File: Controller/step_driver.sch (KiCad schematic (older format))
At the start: 4 parts

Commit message: Minor update to stepper
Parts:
- removed J?: Conn_01x04_Female, symbol Connector:Conn_01x04_Female
- added CN? (x3): CFG1, OPL_Connector:H3-2.54, symbol OPL_Connector:DIP-BLACK-MALE-HEADER-VERT_3P-2.54_
- added J?: Conn_01x04_Male, symbol Connector:Conn_01x04_Male
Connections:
- net labels added: CFG1, CFG2, CFG3
- wire segments 11 -> 14
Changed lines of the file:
@@
 Wire Wire Line
 	3800 2950 3800 3050
-$Comp
-L Connector:Conn_01x04_Female J?
-U 1 1 5D4B72EB
-P 6150 2850
-F 0 "J?" H 6178 2826 50  0000 L CNN
-F 1 "Conn_01x04_Female" H 6178 2735 50  0000 L CNN
-F 2 "" H 6150 2850 50  0001 C CNN
-F 3 "~" H 6150 2850 50  0001 C CNN
-	1    6150 2850
-	1    0    0    -1
-$EndComp
 Wire Wire Line
 	5650 2750 5950 2750
@@
 Wire Wire Line
 	5850 3150 5650 3150
+$Comp
+L Connector:Conn_01x04_Male J?
+U 1 1 5D4B9EAC
+P 6150 2850
+F 0 "J?" H 6122 2824 50  0000 R CNN
+F 1 "Conn_01x04_Male" H 6122 2733 50  0000 R CNN
+F 2 "" H 6150 2850 50  0001 C CNN
+F 3 "~" H 6150 2850 50  0001 C CNN
+	1    6150 2850
+	-1   0    0    -1
+$EndComp
+Text Label 3600 2650 0    31   ~ 0
+CFG1
+Text Label 3600 2750 0    31   ~ 0
+CFG2
+Text Label 3600 2850 0    31   ~ 0
+CFG3
+Wire Wire Line
+	3600 2650 3800 2650
+Wire Wire Line
+	3800 2750 3600 2750
+Wire Wire Line
+	3600 2850 3800 2850
+Text Label 2650 2150 3    31   ~ 0
+CFG1
+Text GLabel 2500 2150 3    31   Input ~ 0
+5V
+$Comp
+L power:GND #PWR?
+U 1 1 5D4BCF63
+P 2800 2150
+F 0 "#PWR?" H 2800 1900 50  0001 C CNN
+F 1 "GND" H 2805 1977 50  0000 C CNN
+F 2 "" H 2800 2150 50  0001 C CNN
+F 3 "" H 2800 2150 50  0001 C CNN
+	1    2800 2150
+	1    0    0    -1
+$EndComp
+$Comp
+L OPL_Connector:DIP-BLACK-MALE-HEADER-VERT_3P-2.54_ CN?
+U 1 1 5D4BDC37
+P 2650 2500
+F 0 "CN?" V 2584 2272 45  0000 R CNN
+F 1 "CFG1" V 2500 2272 45  0000 R CNN
+F 2 "OPL_Connector:H3-2.54" H 2650 2500 50  0001 C CNN
+F 3 "" H 2650 2500 50  0001 C CNN
+F 4 "320020079" H 2680 2650 20  0001 C CNN "SKU"
+	1    2650 2500
+	0    -1   -1   0
+$EndComp
+Text Label 2650 2800 3    31   ~ 0
+CFG2
+Text GLabel 2500 2800 3    31   Input ~ 0
+5V
+$Comp
+L power:GND #PWR?
+U 1 1 5D4BDC43
+P 2800 2800
+F 0 "#PWR?" H 2800 2550 50  0001 C CNN
+F 1 "GND" H 2805 2627 50  0000 C CNN
+F 2 "" H 2800 2800 50  0001 C CNN
+F 3 "" H 2800 2800 50  0001 C CNN
+	1    2800 2800
+	1    0    0    -1
+$EndComp
+$Comp
+L OPL_Connector:DIP-BLACK-MALE-HEADER-VERT_3P-2.54_ CN?
+U 1 1 5D4BEA96
+P 2650 3150
+F 0 "CN?" V 2584 2922 45  0000 R CNN
+F 1 "CFG1" V 2500 2922 45  0000 R CNN
+F 2 "OPL_Connector:H3-2.54" H 2650 3150 50  0001 C CNN
+F 3 "" H 2650 3150 50  0001 C CNN
+F 4 "320020079" H 2680 3300 20  0001 C CNN "SKU"
+	1    2650 3150
+	0    -1   -1   0
+$EndComp
+Text Label 2650 3450 3    31   ~ 0
+CFG3
+Text GLabel 2500 3450 3    31   Input ~ 0
+5V
+$Comp
+L power:GND #PWR?
+U 1 1 5D4BEAA2
+P 2800 3450
+F 0 "#PWR?" H 2800 3200 50  0001 C CNN
+F 1 "GND" H 2805 3277 50  0000 C CNN
+F 2 "" H 2800 3450 50  0001 C CNN
+F 3 "" H 2800 3450 50  0001 C CNN
+	1    2800 3450
+	1    0    0    -1
+$EndComp
+$Comp
+L OPL_Connector:DIP-BLACK-MALE-HEADER-VERT_3P-2.54_ CN?
+U 1 1 5D4BBA78
+P 2650 1850
+F 0 "CN?" V 2584 1622 45  0000 R CNN
+F 1 "CFG1" V 2500 1622 45  0000 R CNN
+F 2 "OPL_Connector:H3-2.54" H 2650 1850 50  0001 C CNN
+F 3 "" H 2650 1850 50  0001 C CNN
+F 4 "320020079" H 2680 2000 20  0001 C CNN "SKU"
+	1    2650 1850
+	0    -1   -1   0
+$EndComp
 $EndSCHEMATC

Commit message: Almost complete schematic
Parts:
- removed J?: Conn_01x04_Male, symbol Connector:Conn_01x04_Male
- added J?: MotorConn, TerminalBlock_Phoenix:TerminalBlock_Phoenix_MPT-0,5-4-2.54_1x04_P2.54mm_Horizontal, symbol Connector:Screw_Terminal_01x04
- C?: value CP1 -> 47uF
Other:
- note added: "!Reset"
- note added: "!Sleep"
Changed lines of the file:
@@
 $Descr A4 11693 8268
 encoding utf-8
-Sheet 3 3
+Sheet 4 4
 Title ""
 Date ""
@@
 U 1 1 5D4B02F5
 P 4100 2900
+AR Path="/5D4AFE00/5D4B02F5" Ref="CN?"  Part="1"
+AR Path="/5D4C0FEF/5D4B02F5" Ref="CN?"  Part="1"
+AR Path="/5D4C1080/5D4B02F5" Ref="CN?"  Part="1"
 F 0 "CN?" H 4228 2942 45  0000 L CNN
 F 1 "FEMALE_LEFT" H 4228 2858 45  0000 L CNN
@@
 U 1 1 5D4B13AD
 P 5350 2900
+AR Path="/5D4AFE00/5D4B13AD" Ref="CN?"  Part="1"
+AR Path="/5D4C0FEF/5D4B13AD" Ref="CN?"  Part="1"
+AR Path="/5D4C1080/5D4B13AD" Ref="CN?"  Part="1"
 F 0 "CN?" H 5700 2950 45  0000 C CNN
 F 1 "FEMALE_RIGHT" H 5700 2850 45  0000 C CNN
@@
 U 1 1 5D4B27F8
 P 5650 2300
+AR Path="/5D4AFE00/5D4B27F8" Ref="C?"  Part="1"
+AR Path="/5D4C0FEF/5D4B27F8" Ref="C?"  Part="1"
+AR Path="/5D4C1080/5D4B27F8" Ref="C?"  Part="1"
 F 0 "C?" H 5535 2254 50  0000 R CNN
-F 1 "CP1" H 5535 2345 50  0000 R CNN
+F 1 "47uF" H 5535 2345 50  0000 R CNN
 F 2 "Capacitor_SMD:CP_Elec_6.3x5.4" H 5650 2300 50  0001 C CNN
 F 3 "~" H 5650 2300 50  0001 C CNN
@@
 U 1 1 5D4B699E
 P 5650 2150
+AR Path="/5D4AFE00/5D4B699E" Ref="#PWR?"  Part="1"
+AR Path="/5D4C0FEF/5D4B699E" Ref="#PWR?"  Part="1"
+AR Path="/5D4C1080/5D4B699E" Ref="#PWR?"  Part="1"
 F 0 "#PWR?" H 5650 1900 50  0001 C CNN
 F 1 "GND" H 5655 1977 50  0000 C CNN
@@
 U 1 1 5D4B88E4
 P 5750 3350
+AR Path="/5D4AFE00/5D4B88E4" Ref="#PWR?"  Part="1"
+AR Path="/5D4C0FEF/5D4B88E4" Ref="#PWR?"  Part="1"
+AR Path="/5D4C1080/5D4B88E4" Ref="#PWR?"  Part="1"
 F 0 "#PWR?" H 5750 3100 50  0001 C CNN
 F 1 "GND" H 5755 3177 50  0000 C CNN
@@
 Wire Wire Line
 	5850 3150 5650 3150
-$Comp
-L Connector:Conn_01x04_Male J?
-U 1 1 5D4B9EAC
-P 6150 2850
-F 0 "J?" H 6122 2824 50  0000 R CNN
-F 1 "Conn_01x04_Male" H 6122 2733 50  0000 R CNN
-F 2 "" H 6150 2850 50  0001 C CNN
-F 3 "~" H 6150 2850 50  0001 C CNN
-	1    6150 2850
-	-1   0    0    -1
-$EndComp
 Text Label 3600 2650 0    31   ~ 0
 CFG1
@@
 U 1 1 5D4BCF63
 P 2800 2150
+AR Path="/5D4AFE00/5D4BCF63" Ref="#PWR?"  Part="1"
+AR Path="/5D4C0FEF/5D4BCF63" Ref="#PWR?"  Part="1"
+AR Path="/5D4C1080/5D4BCF63" Ref="#PWR?"  Part="1"
 F 0 "#PWR?" H 2800 1900 50  0001 C CNN
 F 1 "GND" H 2805 1977 50  0000 C CNN
@@
 U 1 1 5D4BDC37
 P 2650 2500
+AR Path="/5D4AFE00/5D4BDC37" Ref="CN?"  Part="1"
+AR Path="/5D4C0FEF/5D4BDC37" Ref="CN?"  Part="1"
+AR Path="/5D4C1080/5D4BDC37" Ref="CN?"  Part="1"
 F 0 "CN?" V 2584 2272 45  0000 R CNN
 F 1 "CFG1" V 2500 2272 45  0000 R CNN
@@
 U 1 1 5D4BDC43
 P 2800 2800
+AR Path="/5D4AFE00/5D4BDC43" Ref="#PWR?"  Part="1"
+AR Path="/5D4C0FEF/5D4BDC43" Ref="#PWR?"  Part="1"
+AR Path="/5D4C1080/5D4BDC43" Ref="#PWR?"  Part="1"
 F 0 "#PWR?" H 2800 2550 50  0001 C CNN
 F 1 "GND" H 2805 2627 50  0000 C CNN
@@
 U 1 1 5D4BEA96
 P 2650 3150
+AR Path="/5D4AFE00/5D4BEA96" Ref="CN?"  Part="1"
+AR Path="/5D4C0FEF/5D4BEA96" Ref="CN?"  Part="1"
+AR Path="/5D4C1080/5D4BEA96" Ref="CN?"  Part="1"
 F 0 "CN?" V 2584 2922 45  0000 R CNN
 F 1 "CFG1" V 2500 2922 45  0000 R CNN
@@
 U 1 1 5D4BEAA2
 P 2800 3450
+AR Path="/5D4AFE00/5D4BEAA2" Ref="#PWR?"  Part="1"
+AR Path="/5D4C0FEF/5D4BEAA2" Ref="#PWR?"  Part="1"
+AR Path="/5D4C1080/5D4BEAA2" Ref="#PWR?"  Part="1"
 F 0 "#PWR?" H 2800 3200 50  0001 C CNN
 F 1 "GND" H 2805 3277 50  0000 C CNN
@@
 U 1 1 5D4BBA78
 P 2650 1850
+AR Path="/5D4AFE00/5D4BBA78" Ref="CN?"  Part="1"
+AR Path="/5D4C0FEF/5D4BBA78" Ref="CN?"  Part="1"
+AR Path="/5D4C1080/5D4BBA78" Ref="CN?"  Part="1"
 F 0 "CN?" V 2584 1622 45  0000 R CNN
 F 1 "CFG1" V 2500 1622 45  0000 R CNN
@@
 	0    -1   -1   0
 $EndComp
+Text Notes 3650 2950 0    31   ~ 0
+!Reset
+Text Notes 3650 3050 0    31   ~ 0
+!Sleep
+$Comp
+L Connector:Screw_Terminal_01x04 J?
+U 1 1 5D4D9DAD
+P 6150 2850
+AR Path="/5D4D9DAD" Ref="J?"  Part="1"
+AR Path="/5D4AFE00/5D4D9DAD" Ref="J?"  Part="1"
+AR Path="/5D4C1080/5D4D9DAD" Ref="J?"  Part="1"
+F 0 "J?" H 6230 2842 50  0000 L CNN
+F 1 "MotorConn" H 6230 2751 50  0000 L CNN
+F 2 "TerminalBlock_Phoenix:TerminalBlock_Phoenix_MPT-0,5-4-2.54_1x04_P2.54mm_Horizontal" H 6150 2850 50  0001 C CNN
+F 3 "~" H 6150 2850 50  0001 C CNN
+F 4 "320110143" H 6150 2850 50  0001 C CNN "SKU"
+F 5 "GS019-2.54-04P-5" H 6150 2850 50  0001 C CNN "MPN"
+	1    6150 2850
+	1    0    0    -1
+$EndComp
 $EndSCHEMATC

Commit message: Complete schematic
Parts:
- added J?: MotorHeader, symbol OPL_Connector:DIP-BLACK-MALE-HEADER-VERT_4P-2.54_
- CN? (x2): footprint (none) -> OPL_Connector:H8-2.54
- J?: value MotorConn -> MotorTerm
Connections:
- net at CN?.3, J?.1 (Pin_1): now also J?.1 (P$1)
- net at CN?.4, J?.2 (Pin_2): now also J?.2 (P$2)
- net at CN?.5, J?.3 (Pin_3): now also J?.3 (P$3)
- net at CN?.6, J?.4 (Pin_4): now also J?.4 (P$4)
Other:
- note added: "!Enable"
- note added: "CFG1"
- note added: "CFG2"
- note added: "CFG3"
- note added: "Dir"
- note added: "Gnd"
- note added: "MotA+"
- note added: "MotA-"
- note added: "MotB+"
- note added: "MotB-"
- note added: "Step"
- note added: "VMot"
- note added: "Vdd"
- moved on the sheet: J?
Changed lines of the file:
@@
 $Descr A4 11693 8268
 encoding utf-8
-Sheet 4 4
+Sheet 3 4
 Title ""
 Date ""
@@
 AR Path="/5D4C0FEF/5D4B02F5" Ref="CN?"  Part="1"
 AR Path="/5D4C1080/5D4B02F5" Ref="CN?"  Part="1"
-F 0 "CN?" H 4228 2942 45  0000 L CNN
-F 1 "FEMALE_LEFT" H 4228 2858 45  0000 L CNN
-F 2 "" H 4100 2900 50  0001 C CNN
+F 0 "CN?" H 4000 3350 45  0000 L CNN
+F 1 "FEMALE_LEFT" H 4000 2450 45  0000 L CNN
+F 2 "OPL_Connector:H8-2.54" H 4100 2900 50  0001 C CNN
 F 3 "" H 4100 2900 50  0001 C CNN
 F 4 "F185-1108A1BSYC1" H 4130 3050 20  0001 C CNN "MPN"
@@
 AR Path="/5D4C0FEF/5D4B13AD" Ref="CN?"  Part="1"
 AR Path="/5D4C1080/5D4B13AD" Ref="CN?"  Part="1"
-F 0 "CN?" H 5700 2950 45  0000 C CNN
-F 1 "FEMALE_RIGHT" H 5700 2850 45  0000 C CNN
-F 2 "" H 5350 2900 50  0001 C CNN
+F 0 "CN?" H 5300 3350 45  0000 C CNN
+F 1 "FEMALE_RIGHT" H 5500 2450 45  0000 C CNN
+F 2 "OPL_Connector:H8-2.54" H 5350 2900 50  0001 C CNN
 F 3 "" H 5350 2900 50  0001 C CNN
 F 4 "F185-1108A1BSYC1" H 5380 3050 20  0001 C CNN "MPN"
@@
 Wire Wire Line
 	3800 2950 3800 3050
-Wire Wire Line
-	5650 2750 5950 2750
-Wire Wire Line
-	5650 2850 5950 2850
-Wire Wire Line
-	5650 2950 5950 2950
-Wire Wire Line
-	5650 3050 5950 3050
 $Comp
 L power:GND #PWR?
@@
 L Connector:Screw_Terminal_01x04 J?
 U 1 1 5D4D9DAD
-P 6150 2850
+P 6650 2850
 AR Path="/5D4D9DAD" Ref="J?"  Part="1"
 AR Path="/5D4AFE00/5D4D9DAD" Ref="J?"  Part="1"
 AR Path="/5D4C1080/5D4D9DAD" Ref="J?"  Part="1"
-F 0 "J?" H 6230 2842 50  0000 L CNN
-F 1 "MotorConn" H 6230 2751 50  0000 L CNN
-F 2 "TerminalBlock_Phoenix:TerminalBlock_Phoenix_MPT-0,5-4-2.54_1x04_P2.54mm_Horizontal" H 6150 2850 50  0001 C CNN
-F 3 "~" H 6150 2850 50  0001 C CNN
-F 4 "320110143" H 6150 2850 50  0001 C CNN "SKU"
-F 5 "GS019-2.54-04P-5" H 6150 2850 50  0001 C CNN "MPN"
-	1    6150 2850
-	1    0    0    -1
-$EndComp
+F 0 "J?" H 6730 2842 50  0000 L CNN
+F 1 "MotorTerm" H 6730 2751 50  0000 L CNN
+F 2 "TerminalBlock_Phoenix:TerminalBlock_Phoenix_MPT-0,5-4-2.54_1x04_P2.54mm_Horizontal" H 6650 2850 50  0001 C CNN
+F 3 "~" H 6650 2850 50  0001 C CNN
+F 4 "320110143" H 6650 2850 50  0001 C CNN "SKU"
+F 5 "GS019-2.54-04P-5" H 6650 2850 50  0001 C CNN "MPN"
+	1    6650 2850
+	1    0    0    -1
+$EndComp
+$Comp
+L OPL_Connector:DIP-BLACK-MALE-HEADER-VERT_4P-2.54_ J?
+U 1 1 5D567ECA
+P 6750 3450
+F 0 "J?" H 6878 3492 45  0000 L CNN
+F 1 "MotorHeader" H 6878 3408 45  0000 L CNN
+F 2 "" H 6750 3450 50  0001 C CNN
+F 3 "" H 6750 3450 50  0001 C CNN
+F 4 "P125-1104A0BS116A1" H 6780 3600 20  0001 C CNN "MPN"
+F 5 "320020017" H 6780 3600 20  0001 C CNN "SKU"
+	1    6750 3450
+	1    0    0    -1
+$EndComp
+Wire Wire Line
+	5650 2750 6350 2750
+Wire Wire Line
+	6350 2750 6350 3300
+Wire Wire Line
+	6350 3300 6450 3300
+Connection ~ 6350 2750
+Wire Wire Line
+	6350 2750 6450 2750
+Wire Wire Line
+	5650 2850 6300 2850
+Wire Wire Line
+	6300 2850 6300 3400
+Wire Wire Line
+	6300 3400 6450 3400
+Connection ~ 6300 2850
+Wire Wire Line
+	6300 2850 6450 2850
+Wire Wire Line
+	5650 2950 6250 2950
+Wire Wire Line
+	6250 2950 6250 3500
+Wire Wire Line
+	6250 3500 6450 3500
+Connection ~ 6250 2950
+Wire Wire Line
+	6250 2950 6450 2950
+Wire Wire Line
+	5650 3050 6200 3050
+Wire Wire Line
+	6200 3050 6200 3600
+Wire Wire Line
+	6200 3600 6450 3600
+Connection ~ 6200 3050
+Wire Wire Line
+	6200 3050 6450 3050
+Text Notes 4250 2550 0    39   ~ 0
+!Enable
+Text Notes 4250 2650 0    39   ~ 0
+CFG1
+Text Notes 4250 2750 0    39   ~ 0
+CFG2
+Text Notes 4250 2850 0    39   ~ 0
+CFG3
+Text Notes 4250 2950 0    39   ~ 0
+!Reset
+Text Notes 4250 3050 0    39   ~ 0
+!Sleep
+Text Notes 4250 3150 0    39   ~ 0
+Step
+Text Notes 4250 3250 0    39   ~ 0
+Dir
+Text Notes 5000 2550 0    39   ~ 0
+VMot
+Text Notes 5000 2650 0    39   ~ 0
+Gnd
+Text Notes 5000 2750 0    39   ~ 0
+MotB-
+Text Notes 5000 2850 0    39   ~ 0
+MotB+
+Text Notes 5000 2950 0    39   ~ 0
+MotA-
+Text Notes 5000 3050 0    39   ~ 0
+MotA+
+Text Notes 5000 3150 0    39   ~ 0
+Vdd
+Text Notes 5000 3250 0    39   ~ 0
+Gnd
 $EndSCHEMATC

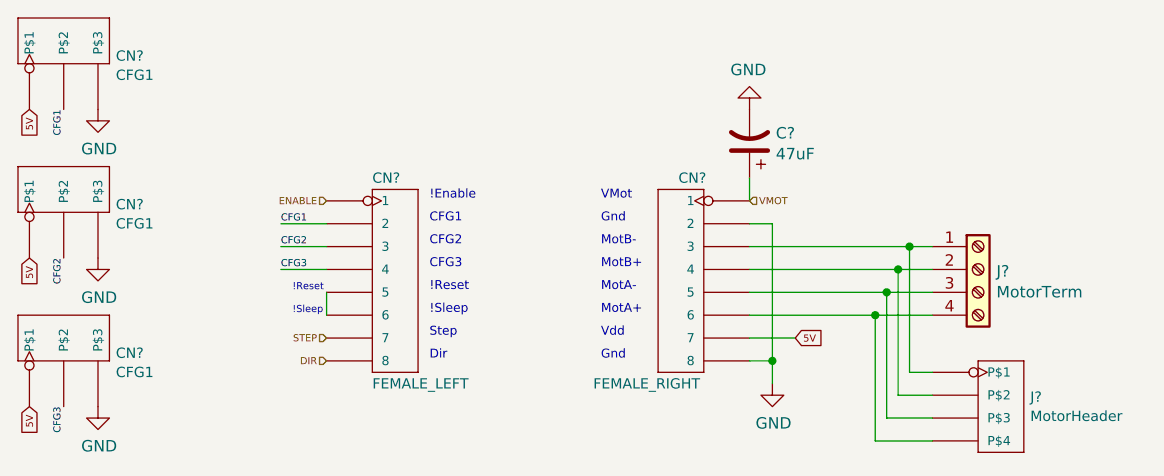
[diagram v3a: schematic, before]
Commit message: Set more footprints
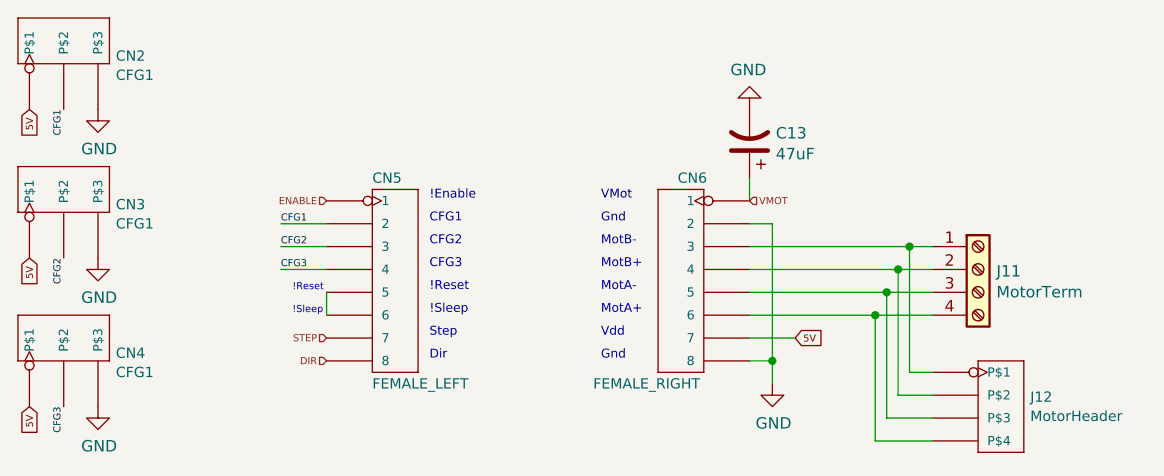
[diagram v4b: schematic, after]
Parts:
- J12: renamed from J?; footprint (none) -> OPL_Connector:H4-2.54
- gave numbers to parts that had none: 7
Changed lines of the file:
@@
 $EndDescr
 $Comp
-L OPL_Connector:DIP-BLACK-FEMALE-HEADER-VERT_8P-2.54_ CN?
+L OPL_Connector:DIP-BLACK-FEMALE-HEADER-VERT_8P-2.54_ CN5
 U 1 1 5D4B02F5
 P 4100 2900
-AR Path="/5D4AFE00/5D4B02F5" Ref="CN?"  Part="1"
+AR Path="/5D4AFE00/5D4B02F5" Ref="CN5"  Part="1"
 AR Path="/5D4C0FEF/5D4B02F5" Ref="CN?"  Part="1"
-AR Path="/5D4C1080/5D4B02F5" Ref="CN?"  Part="1"
-F 0 "CN?" H 4000 3350 45  0000 L CNN
+AR Path="/5D4C1080/5D4B02F5" Ref="CN10"  Part="1"
+F 0 "CN5" H 4000 3350 45  0000 L CNN
 F 1 "FEMALE_LEFT" H 4000 2450 45  0000 L CNN
 F 2 "OPL_Connector:H8-2.54" H 4100 2900 50  0001 C CNN
@@
 $EndComp
 $Comp
-L OPL_Connector:DIP-BLACK-FEMALE-HEADER-VERT_8P-2.54_ CN?
+L OPL_Connector:DIP-BLACK-FEMALE-HEADER-VERT_8P-2.54_ CN6
 U 1 1 5D4B13AD
 P 5350 2900
-AR Path="/5D4AFE00/5D4B13AD" Ref="CN?"  Part="1"
+AR Path="/5D4AFE00/5D4B13AD" Ref="CN6"  Part="1"
 AR Path="/5D4C0FEF/5D4B13AD" Ref="CN?"  Part="1"
-AR Path="/5D4C1080/5D4B13AD" Ref="CN?"  Part="1"
-F 0 "CN?" H 5300 3350 45  0000 C CNN
+AR Path="/5D4C1080/5D4B13AD" Ref="CN11"  Part="1"
+F 0 "CN6" H 5300 3350 45  0000 C CNN
 F 1 "FEMALE_RIGHT" H 5500 2450 45  0000 C CNN
 F 2 "OPL_Connector:H8-2.54" H 5350 2900 50  0001 C CNN
@@
 VMOT
 $Comp
-L Device:CP1 C?
+L Device:CP1 C13
 U 1 1 5D4B27F8
 P 5650 2300
-AR Path="/5D4AFE00/5D4B27F8" Ref="C?"  Part="1"
+AR Path="/5D4AFE00/5D4B27F8" Ref="C13"  Part="1"
 AR Path="/5D4C0FEF/5D4B27F8" Ref="C?"  Part="1"
-AR Path="/5D4C1080/5D4B27F8" Ref="C?"  Part="1"
-F 0 "C?" H 5535 2254 50  0000 R CNN
+AR Path="/5D4C1080/5D4B27F8" Ref="C14"  Part="1"
+F 0 "C13" H 5535 2254 50  0000 R CNN
 F 1 "47uF" H 5535 2345 50  0000 R CNN
 F 2 "Capacitor_SMD:CP_Elec_6.3x5.4" H 5650 2300 50  0001 C CNN
@@
 	5650 2550 5650 2450
 $Comp
-L power:GND #PWR?
+L power:GND #PWR026
 U 1 1 5D4B699E
 P 5650 2150
-AR Path="/5D4AFE00/5D4B699E" Ref="#PWR?"  Part="1"
+AR Path="/5D4AFE00/5D4B699E" Ref="#PWR026"  Part="1"
 AR Path="/5D4C0FEF/5D4B699E" Ref="#PWR?"  Part="1"
-AR Path="/5D4C1080/5D4B699E" Ref="#PWR?"  Part="1"
-F 0 "#PWR?" H 5650 1900 50  0001 C CNN
+AR Path="/5D4C1080/5D4B699E" Ref="#PWR031"  Part="1"
+F 0 "#PWR026" H 5650 1900 50  0001 C CNN
 F 1 "GND" H 5655 1977 50  0000 C CNN
 F 2 "" H 5650 2150 50  0001 C CNN
@@
 	3800 2950 3800 3050
 $Comp
-L power:GND #PWR?
+L power:GND #PWR027
 U 1 1 5D4B88E4
 P 5750 3350
-AR Path="/5D4AFE00/5D4B88E4" Ref="#PWR?"  Part="1"
+AR Path="/5D4AFE00/5D4B88E4" Ref="#PWR027"  Part="1"
 AR Path="/5D4C0FEF/5D4B88E4" Ref="#PWR?"  Part="1"
-AR Path="/5D4C1080/5D4B88E4" Ref="#PWR?"  Part="1"
-F 0 "#PWR?" H 5750 3100 50  0001 C CNN
+AR Path="/5D4C1080/5D4B88E4" Ref="#PWR032"  Part="1"
+F 0 "#PWR027" H 5750 3100 50  0001 C CNN
 F 1 "GND" H 5755 3177 50  0000 C CNN
 F 2 "" H 5750 3350 50  0001 C CNN
@@
 5V
 $Comp
-L power:GND #PWR?
+L power:GND #PWR023
 U 1 1 5D4BCF63
 P 2800 2150
-AR Path="/5D4AFE00/5D4BCF63" Ref="#PWR?"  Part="1"
+AR Path="/5D4AFE00/5D4BCF63" Ref="#PWR023"  Part="1"
 AR Path="/5D4C0FEF/5D4BCF63" Ref="#PWR?"  Part="1"
-AR Path="/5D4C1080/5D4BCF63" Ref="#PWR?"  Part="1"
-F 0 "#PWR?" H 2800 1900 50  0001 C CNN
+AR Path="/5D4C1080/5D4BCF63" Ref="#PWR028"  Part="1"
+F 0 "#PWR023" H 2800 1900 50  0001 C CNN
 F 1 "GND" H 2805 1977 50  0000 C CNN
 F 2 "" H 2800 2150 50  0001 C CNN
@@
 $EndComp
 $Comp
-L OPL_Connector:DIP-BLACK-MALE-HEADER-VERT_3P-2.54_ CN?
+L OPL_Connector:DIP-BLACK-MALE-HEADER-VERT_3P-2.54_ CN3
 U 1 1 5D4BDC37
 P 2650 2500
-AR Path="/5D4AFE00/5D4BDC37" Ref="CN?"  Part="1"
+AR Path="/5D4AFE00/5D4BDC37" Ref="CN3"  Part="1"
 AR Path="/5D4C0FEF/5D4BDC37" Ref="CN?"  Part="1"
-AR Path="/5D4C1080/5D4BDC37" Ref="CN?"  Part="1"
-F 0 "CN?" V 2584 2272 45  0000 R CNN
+AR Path="/5D4C1080/5D4BDC37" Ref="CN8"  Part="1"
+F 0 "CN3" V 2584 2272 45  0000 R CNN
 F 1 "CFG1" V 2500 2272 45  0000 R CNN
 F 2 "OPL_Connector:H3-2.54" H 2650 2500 50  0001 C CNN
@@
 5V
 $Comp
-L power:GND #PWR?
+L power:GND #PWR024
 U 1 1 5D4BDC43
 P 2800 2800
-AR Path="/5D4AFE00/5D4BDC43" Ref="#PWR?"  Part="1"
+AR Path="/5D4AFE00/5D4BDC43" Ref="#PWR024"  Part="1"
 AR Path="/5D4C0FEF/5D4BDC43" Ref="#PWR?"  Part="1"
-AR Path="/5D4C1080/5D4BDC43" Ref="#PWR?"  Part="1"
-F 0 "#PWR?" H 2800 2550 50  0001 C CNN
+AR Path="/5D4C1080/5D4BDC43" Ref="#PWR029"  Part="1"
+F 0 "#PWR024" H 2800 2550 50  0001 C CNN
 F 1 "GND" H 2805 2627 50  0000 C CNN
 F 2 "" H 2800 2800 50  0001 C CNN
@@
 $EndComp
 $Comp
-L OPL_Connector:DIP-BLACK-MALE-HEADER-VERT_3P-2.54_ CN?
+L OPL_Connector:DIP-BLACK-MALE-HEADER-VERT_3P-2.54_ CN4
 U 1 1 5D4BEA96
 P 2650 3150
-AR Path="/5D4AFE00/5D4BEA96" Ref="CN?"  Part="1"
+AR Path="/5D4AFE00/5D4BEA96" Ref="CN4"  Part="1"
 AR Path="/5D4C0FEF/5D4BEA96" Ref="CN?"  Part="1"
-AR Path="/5D4C1080/5D4BEA96" Ref="CN?"  Part="1"
-F 0 "CN?" V 2584 2922 45  0000 R CNN
+AR Path="/5D4C1080/5D4BEA96" Ref="CN9"  Part="1"
+F 0 "CN4" V 2584 2922 45  0000 R CNN
 F 1 "CFG1" V 2500 2922 45  0000 R CNN
 F 2 "OPL_Connector:H3-2.54" H 2650 3150 50  0001 C CNN
@@
 5V
 $Comp
-L power:GND #PWR?
+L power:GND #PWR025
 U 1 1 5D4BEAA2
 P 2800 3450
-AR Path="/5D4AFE00/5D4BEAA2" Ref="#PWR?"  Part="1"
+AR Path="/5D4AFE00/5D4BEAA2" Ref="#PWR025"  Part="1"
 AR Path="/5D4C0FEF/5D4BEAA2" Ref="#PWR?"  Part="1"
-AR Path="/5D4C1080/5D4BEAA2" Ref="#PWR?"  Part="1"
-F 0 "#PWR?" H 2800 3200 50  0001 C CNN
+AR Path="/5D4C1080/5D4BEAA2" Ref="#PWR030"  Part="1"
+F 0 "#PWR025" H 2800 3200 50  0001 C CNN
 F 1 "GND" H 2805 3277 50  0000 C CNN
 F 2 "" H 2800 3450 50  0001 C CNN
@@
 $EndComp
 $Comp
-L OPL_Connector:DIP-BLACK-MALE-HEADER-VERT_3P-2.54_ CN?
+L OPL_Connector:DIP-BLACK-MALE-HEADER-VERT_3P-2.54_ CN2
 U 1 1 5D4BBA78
 P 2650 1850
-AR Path="/5D4AFE00/5D4BBA78" Ref="CN?"  Part="1"
+AR Path="/5D4AFE00/5D4BBA78" Ref="CN2"  Part="1"
 AR Path="/5D4C0FEF/5D4BBA78" Ref="CN?"  Part="1"
-AR Path="/5D4C1080/5D4BBA78" Ref="CN?"  Part="1"
-F 0 "CN?" V 2584 1622 45  0000 R CNN
+AR Path="/5D4C1080/5D4BBA78" Ref="CN7"  Part="1"
+F 0 "CN2" V 2584 1622 45  0000 R CNN
 F 1 "CFG1" V 2500 1622 45  0000 R CNN
 F 2 "OPL_Connector:H3-2.54" H 2650 1850 50  0001 C CNN
@@
 P 6650 2850
 AR Path="/5D4D9DAD" Ref="J?"  Part="1"
-AR Path="/5D4AFE00/5D4D9DAD" Ref="J?"  Part="1"
-AR Path="/5D4C1080/5D4D9DAD" Ref="J?"  Part="1"
-F 0 "J?" H 6730 2842 50  0000 L CNN
+AR Path="/5D4AFE00/5D4D9DAD" Ref="J11"  Part="1"
+AR Path="/5D4C1080/5D4D9DAD" Ref="J13"  Part="1"
+F 0 "J11" H 6730 2842 50  0000 L CNN
 F 1 "MotorTerm" H 6730 2751 50  0000 L CNN
 F 2 "TerminalBlock_Phoenix:TerminalBlock_Phoenix_MPT-0,5-4-2.54_1x04_P2.54mm_Horizontal" H 6650 2850 50  0001 C CNN
@@
 $EndComp
 $Comp
-L OPL_Connector:DIP-BLACK-MALE-HEADER-VERT_4P-2.54_ J?
+L OPL_Connector:DIP-BLACK-MALE-HEADER-VERT_4P-2.54_ J12
 U 1 1 5D567ECA
 P 6750 3450
-F 0 "J?" H 6878 3492 45  0000 L CNN
+AR Path="/5D4AFE00/5D567ECA" Ref="J12"  Part="1"
+AR Path="/5D4C1080/5D567ECA" Ref="J14"  Part="1"
+F 0 "J12" H 6878 3492 45  0000 L CNN
 F 1 "MotorHeader" H 6878 3408 45  0000 L CNN
-F 2 "" H 6750 3450 50  0001 C CNN
+F 2 "OPL_Connector:H4-2.54" H 6750 3450 50  0001 C CNN
 F 3 "" H 6750 3450 50  0001 C CNN
 F 4 "P125-1104A0BS116A1" H 6780 3600 20  0001 C CNN "MPN"
